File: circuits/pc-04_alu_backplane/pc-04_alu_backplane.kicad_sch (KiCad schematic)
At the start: 16 parts, among them U1 74HC273, U2 74HC244, U3 74HC244, U4 74HC138, U5 4081, U6 4011, U7 4071, U8 74HC74, U9 4011

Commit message: Kicad upgrade to 9.0
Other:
- title: PC-01 Dual Register Unit -> PC-04 ALU Backplane

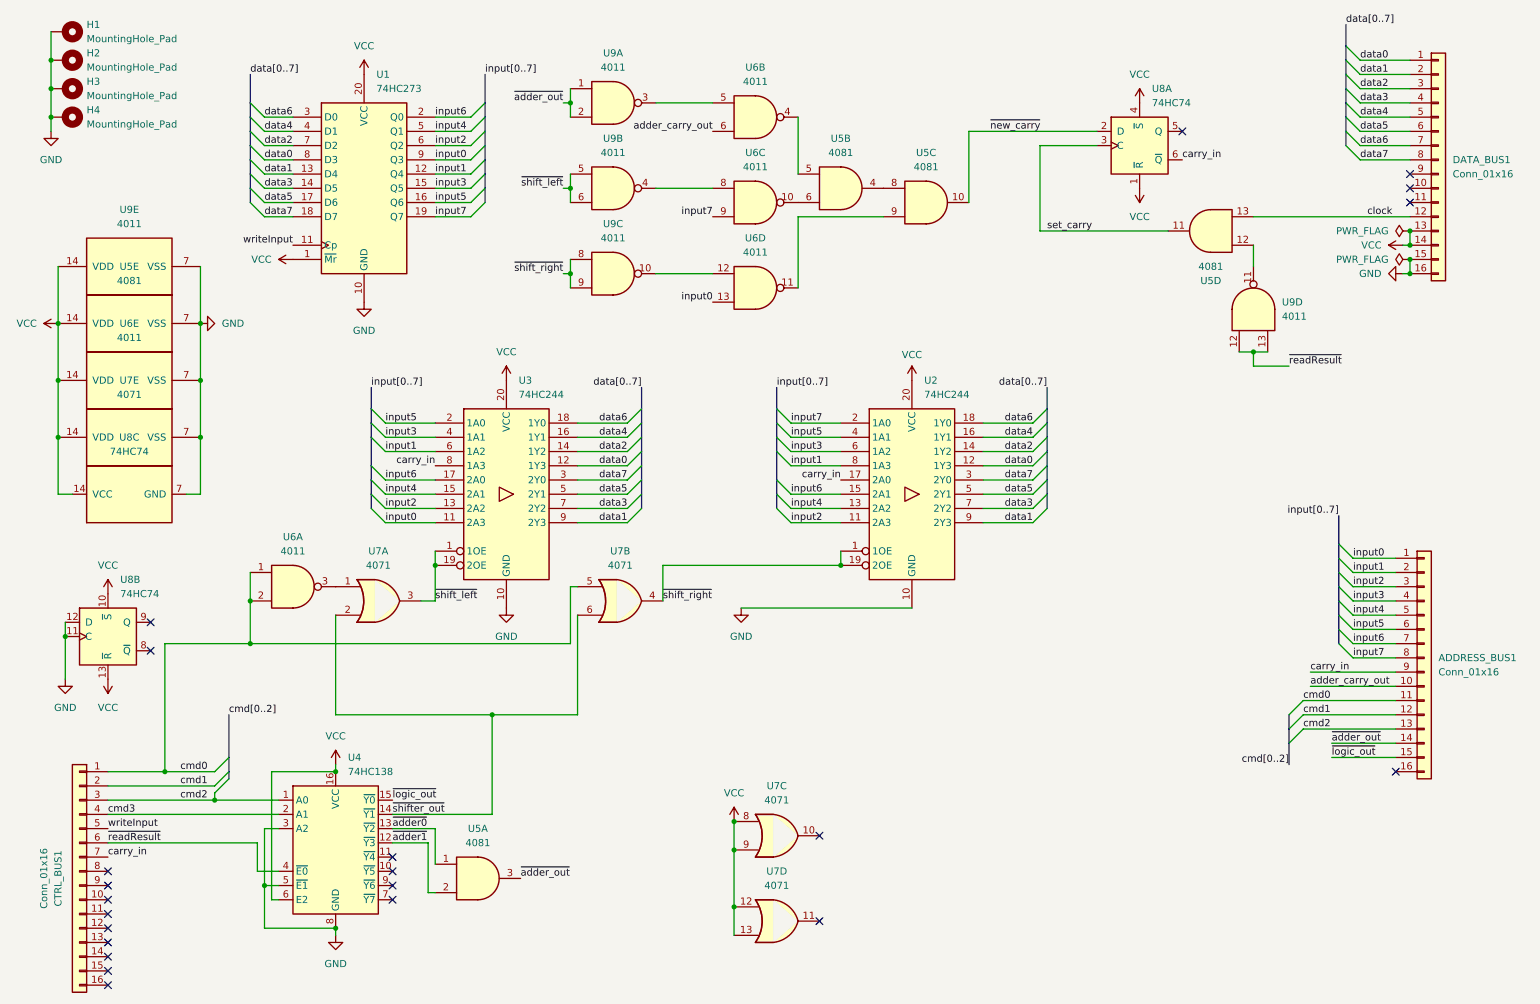
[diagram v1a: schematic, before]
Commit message: pc-04: add missing pull-up resistors
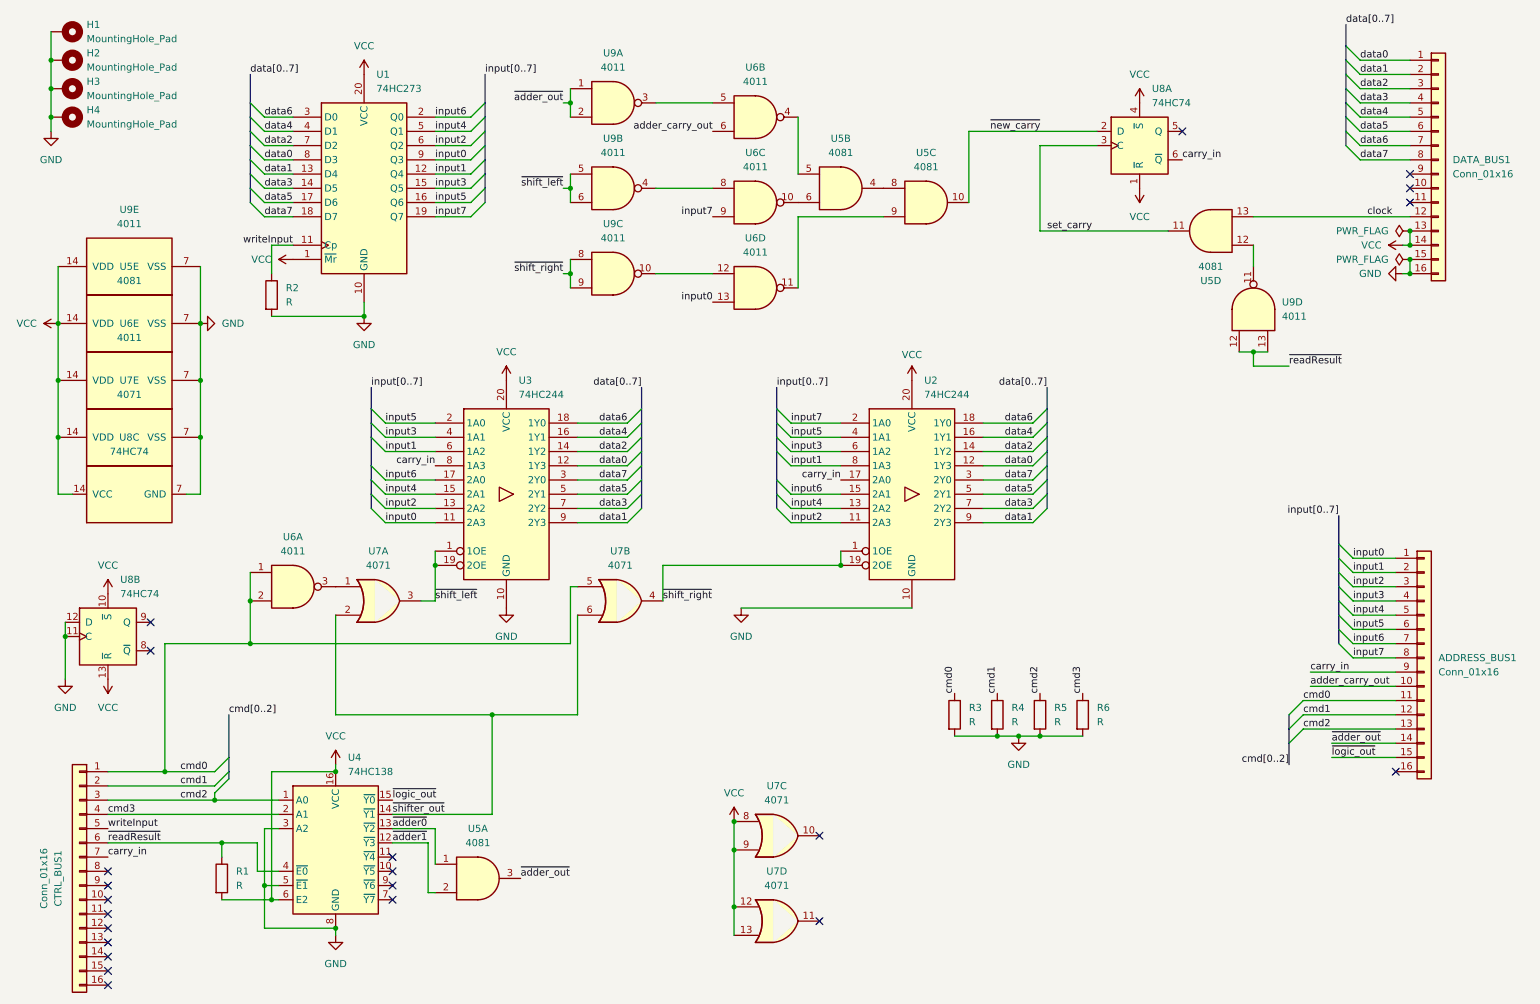
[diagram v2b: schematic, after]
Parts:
- added R1, R2, R3, R4, R5, R6: R, Resistor_SMD:R_0603_1608Metric, symbol Device:R
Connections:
- net GND: now also R2.2, R3.2, R4.2, R5.2, R6.2
- net VCC: now also R1.2
- net cmd0: now also R3.1
- net cmd1: now also R4.1
- net cmd2: now also R5.1
- net cmd3: now also R6.1
- net writeInput: now also R2.1
- net ~{readResult}: now also R1.1

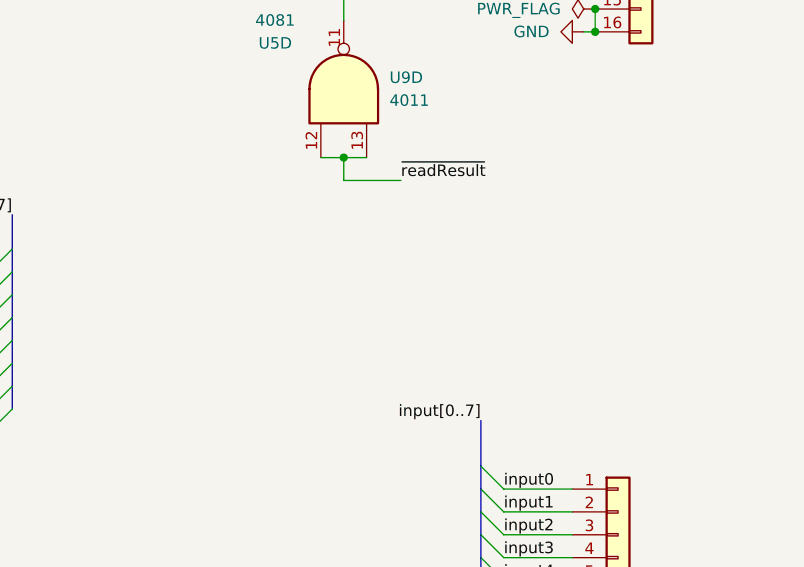
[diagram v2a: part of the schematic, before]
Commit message: add filter and decoupling capacitors to all boards
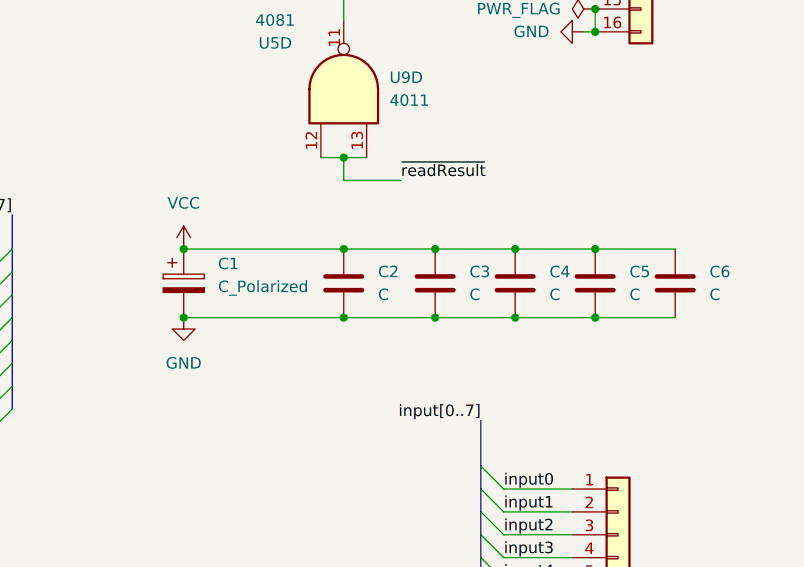
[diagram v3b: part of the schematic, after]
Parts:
- added C1: C_Polarized, Capacitor_SMD:CP_Elec_5x5.3, symbol Device:C_Polarized
- added C2, C3, C4, C5, C6: C, Capacitor_SMD:C_0603_1608Metric, symbol Device:C
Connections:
- net GND: now also C1.2, C2.2, C3.2, C4.2, C5.2, C6.2
- net VCC: now also C1.1, C2.1, C3.1, C4.1, C5.1, C6.1
